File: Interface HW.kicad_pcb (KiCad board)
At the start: 2 copper layers, 101.6 x 50.8 mm, 79 parts, among them J1 CONN_8, J2 CONN_8, J3 CONN_8, J4 CONN_8, J5 TE: 640456-3, J6 CONN_13X2, J7 TERM_3, J8 TERM-3, P1 CONNECTOR_2, Q1 2N7002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

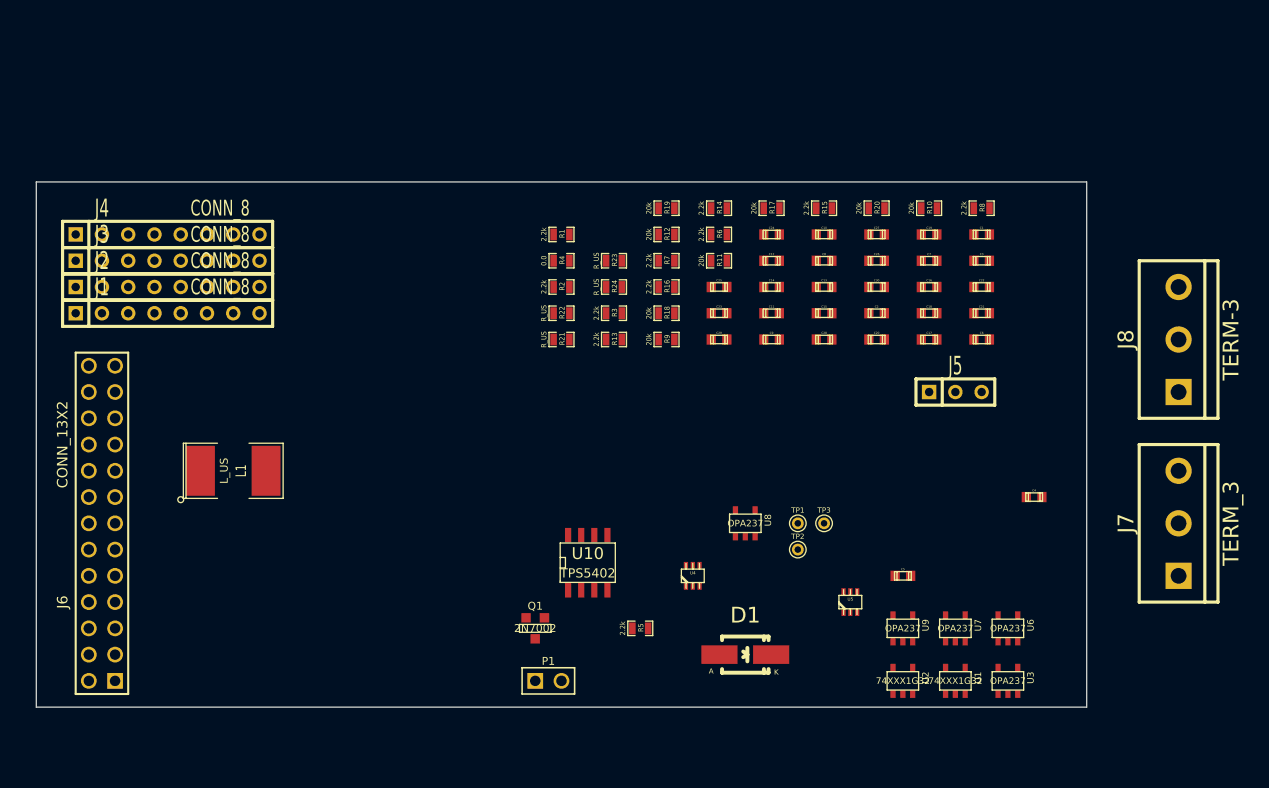
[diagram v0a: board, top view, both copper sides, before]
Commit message: Changed PCB size to 5x5cm, got most components placed
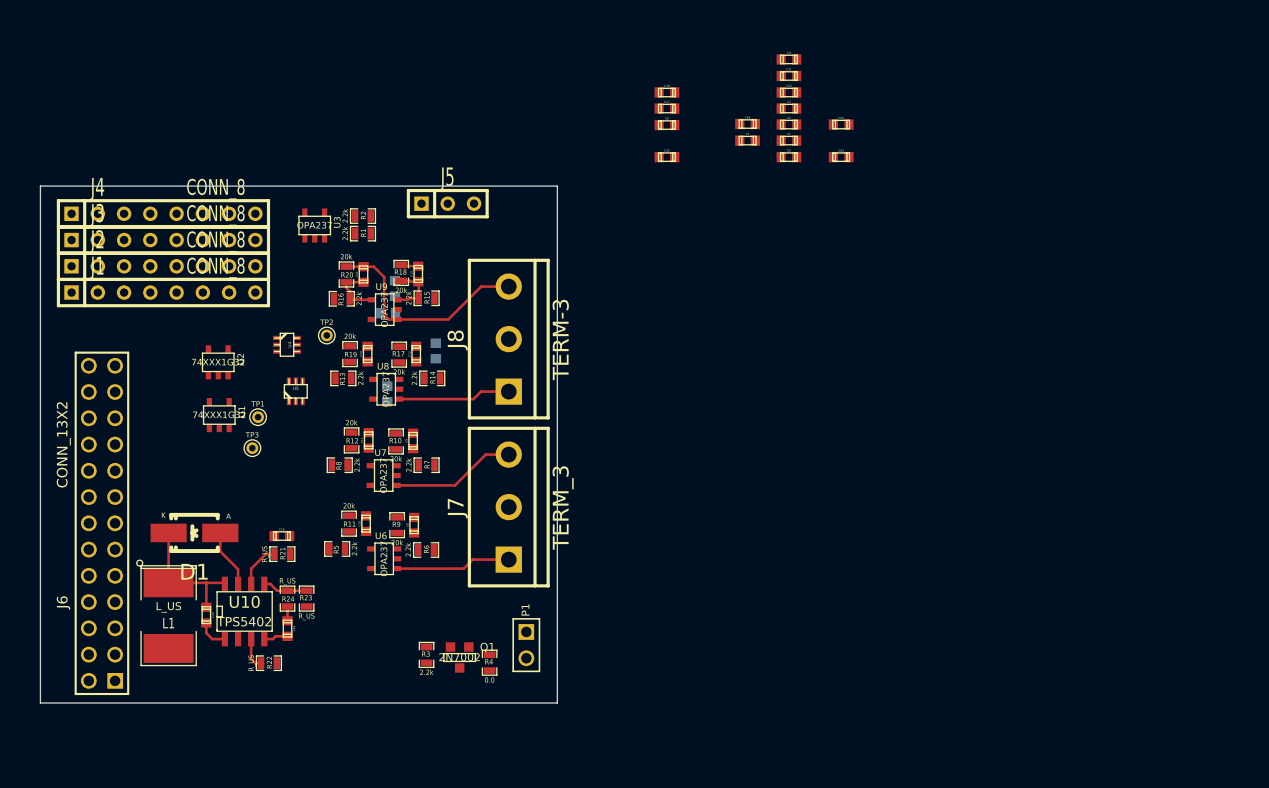
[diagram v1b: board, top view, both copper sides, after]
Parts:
- C27, C28, C29, C30: moved to B.Cu
- moved U3 80.2 mm to (128.5, 105.8)
- moved U1 75.7 mm to (119.3, 124.2)
- moved U2 73.0 mm to (119.2, 119.0)
- moved C19 72.8 mm to (125.9, 144.8), turned to 270 degrees
- moved C20 70.1 mm to (118.0, 143.5), turned to 270 degrees
- moved C16 67.1 mm to (125.3, 135.8)
- moved R8 66.9 mm to (130.9, 129.0), turned to 180 degrees
- moved J7 64.8 mm to (147.3, 133.1)
- moved J8 64.8 mm to (147.3, 116.8)
- moved U6 60.7 mm to (135.2, 138.1), turned to 90 degrees
- moved U9 58.8 mm to (135.3, 114.0), turned to 90 degrees
- moved U5 57.4 mm to (126.7, 121.8)
- moved U7 57.2 mm to (135.2, 130.0), turned to 90 degrees
- moved R10 56.3 mm to (136.4, 126.7), turned to 90 degrees
- moved TP3 55.8 mm to (122.5, 127.3)
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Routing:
- net N-0000062: track 0.00 -> 21.3 mm
- net N-0000069: track 0.00 -> 12.8 mm
- net N-0000055: track 0.00 -> 12.1 mm
- net N-0000061: track 0.00 -> 11.1 mm
- net N-0000067: track 0.00 -> 10.9 mm
- net GND: track 0.00 -> 8.77 mm
- net N-0000065: track 0.00 -> 5.56 mm
- net N-0000063: track 0.00 -> 5.38 mm
- net N-0000070: track 0.00 -> 4.37 mm
- net N-0000071: track 0.00 -> 4.31 mm
- net N-0000072: track 0.00 -> 3.04 mm
- net N-0000068: track 0.00 -> 3.03 mm
- net N-0000073: track 0.00 -> 2.35 mm
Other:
- board size 101.6 x 50.8 mm -> 50 x 50 mm

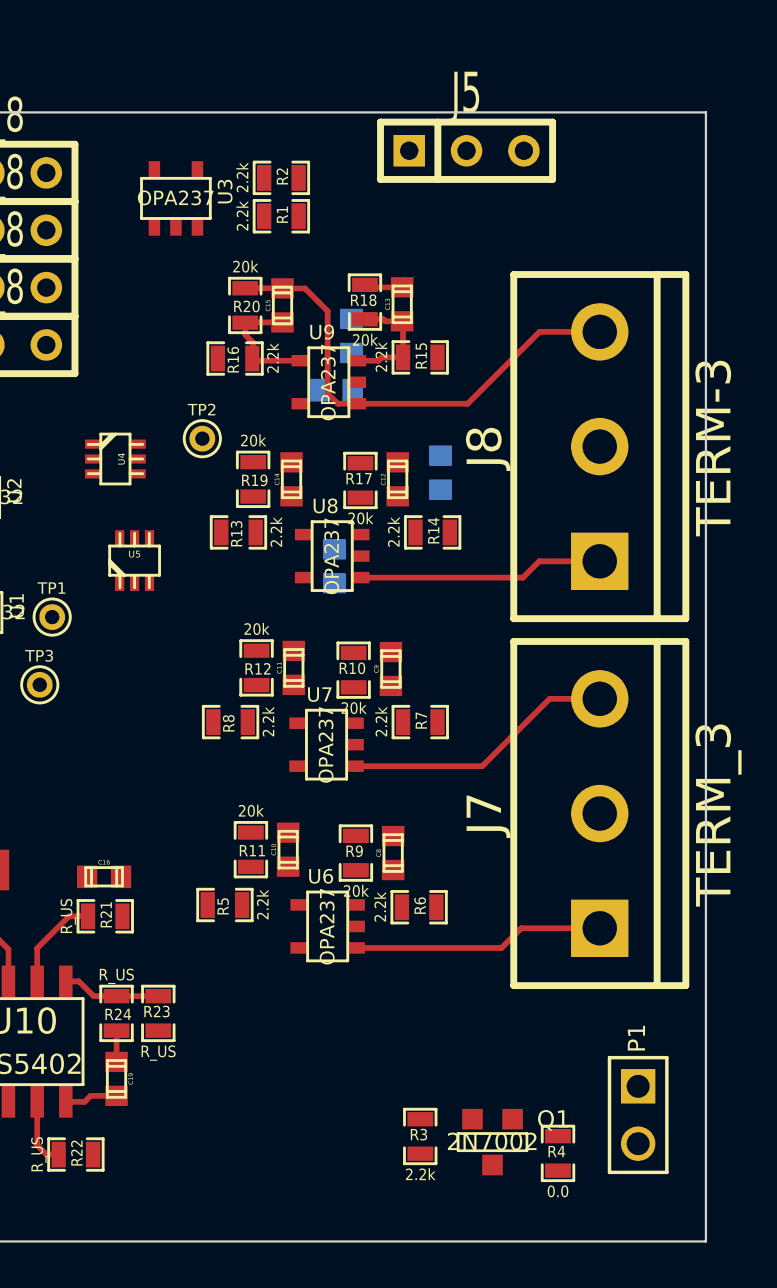
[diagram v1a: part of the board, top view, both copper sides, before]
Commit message: Added a cap to ref, chages buck converter caps, more routing, didn't pull in netlist
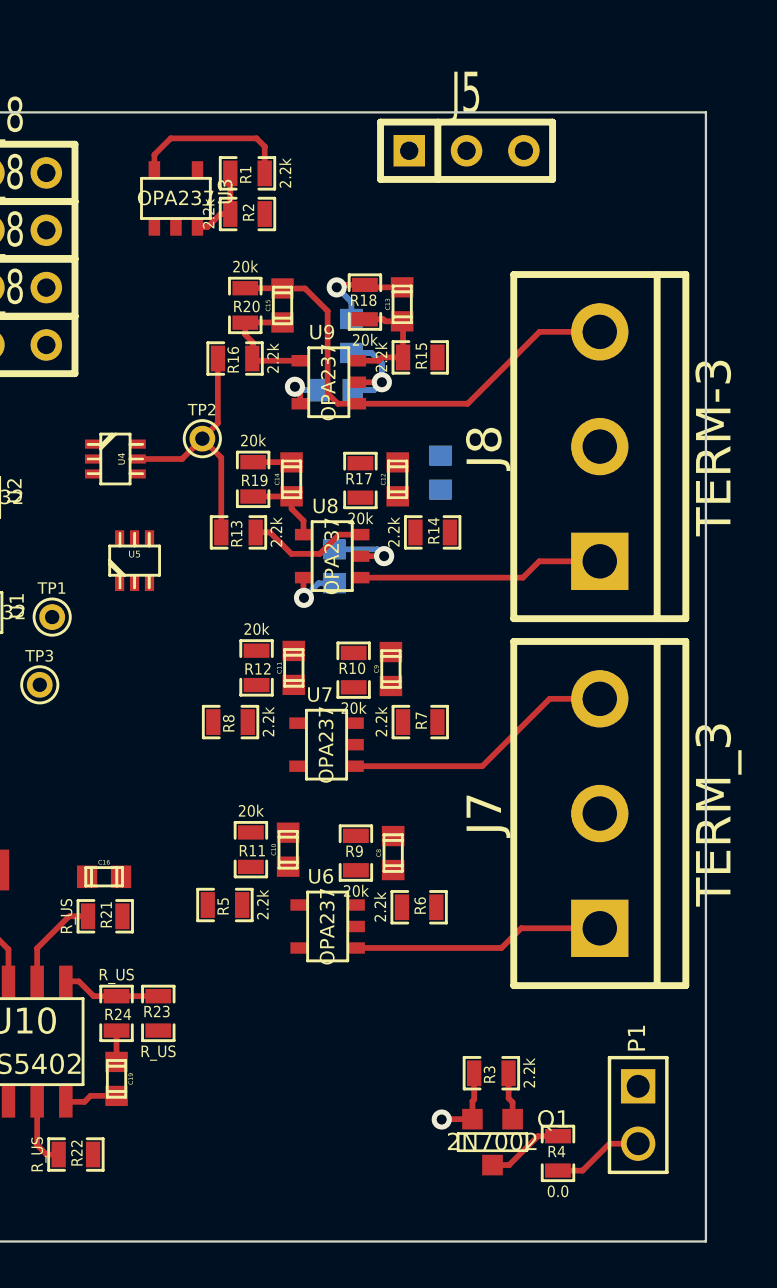
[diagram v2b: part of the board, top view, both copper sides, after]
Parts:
- moved R3 4.21 mm to (142.5, 144.6), turned to 180 degrees
- moved R1 2.42 mm to (131.7, 104.7), turned to 180 degrees
- moved R2 2.19 mm to (131.7, 106.5)
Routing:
- net DAC_Y: track 0.00 -> 11.5 mm
- net -15V: track 0.00 -> 8.26 mm, vias 0 -> 2
- net 3V3: track 0.00 -> 7.19 mm
- net GND: track 8.77 -> 15.4 mm, vias 0 -> 2
- net N-0000064: track 0.00 -> 5.40 mm
- net +15V: track 0.00 -> 4.48 mm, vias 0 -> 2
- net N-0000025: track 0.00 -> 4.04 mm
- net N-0000066: track 0.00 -> 3.62 mm
- net N-0000054: track 0.00 -> 3.50 mm
- net N-0000024: track 0.00 -> 3.43 mm
- net /Interface HW-01/GPIO_12: track 0.00 -> 2.11 mm
- net N-0000067: track 10.9 -> 12.6 mm

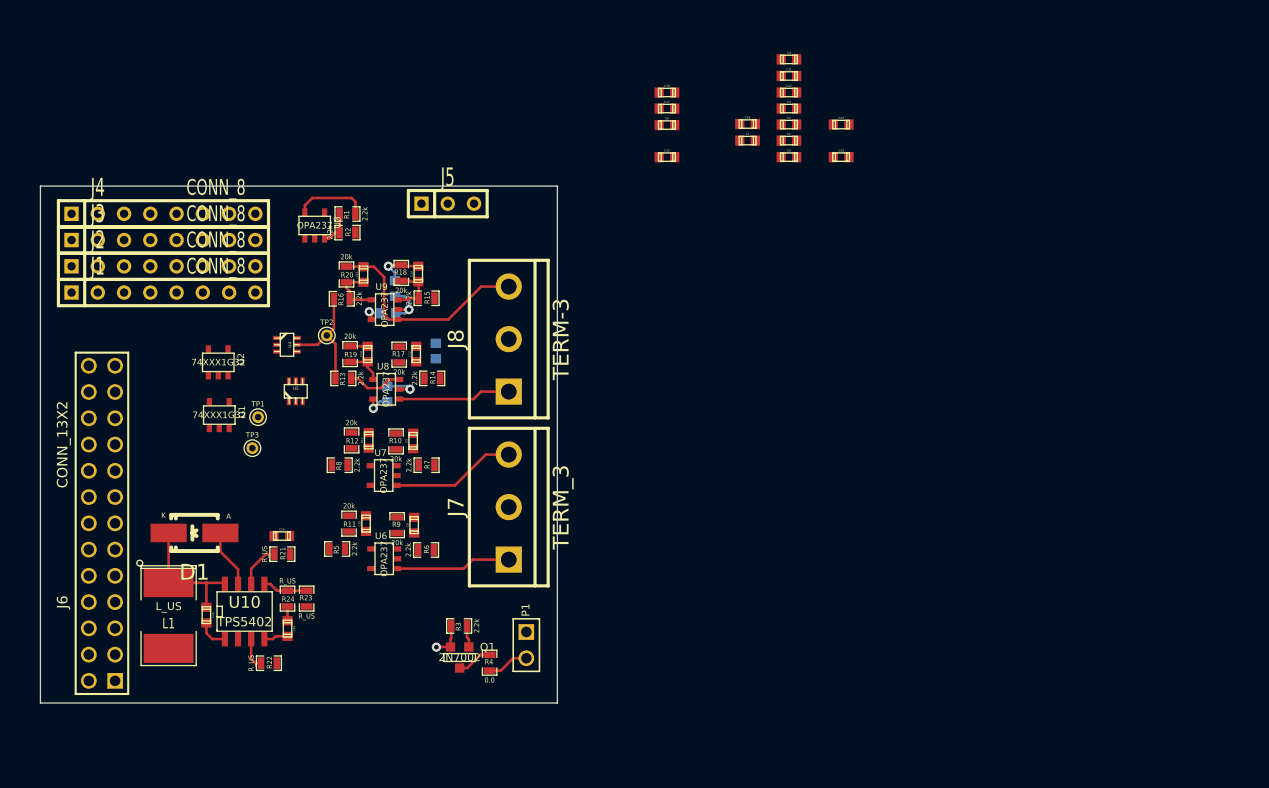
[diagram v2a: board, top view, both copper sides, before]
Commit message: More routing, added power supply test points, added mounting holes
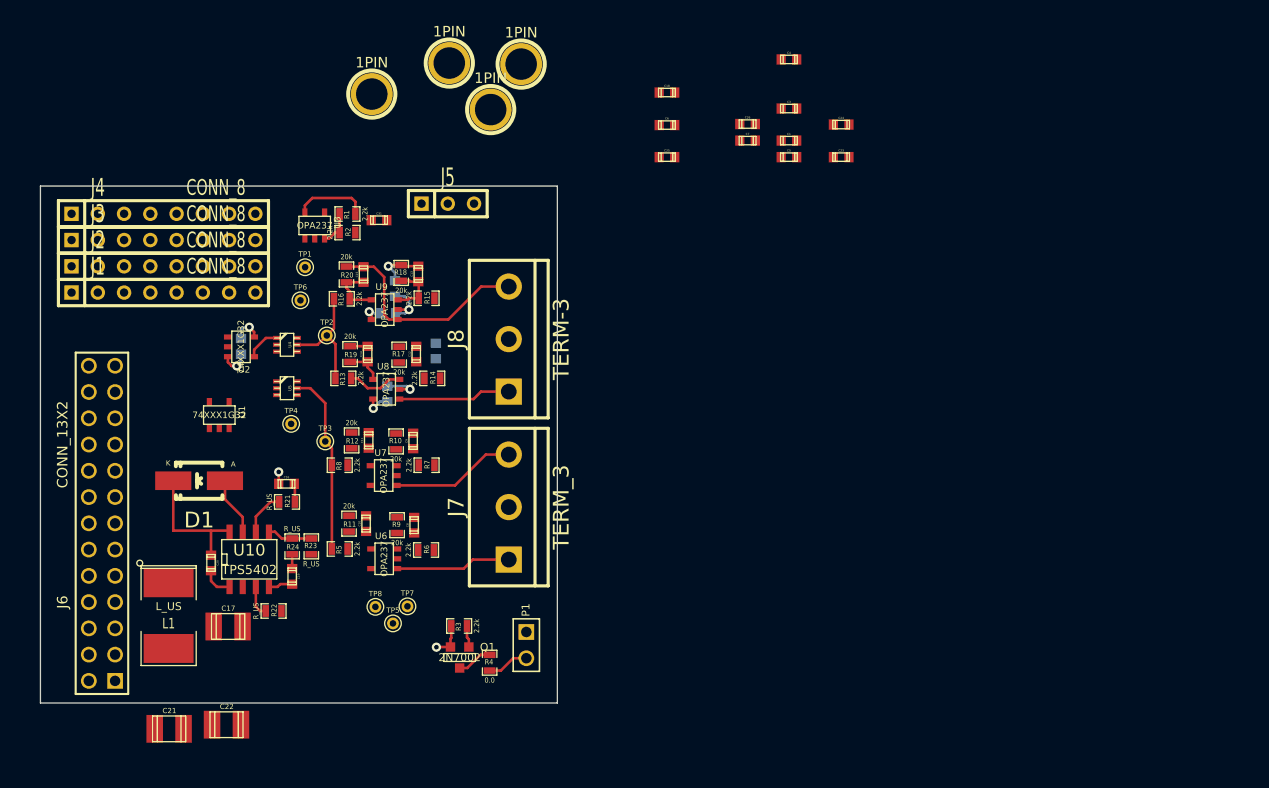
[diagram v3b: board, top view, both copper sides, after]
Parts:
- added 1PIN: P***, 1pin, F.Cu at (134.1, 93.1)
- added 1PIN: P***, 1pin, F.Cu at (141.6, 90.1)
- added 1PIN: P***, 1pin, F.Cu at (148.5, 90.2)
- added 1PIN: P***, 1pin, F.Cu at (145.6, 94.6)
- added C31: 0.1uF, c_0603, F.Cu at (134.8, 105.3)
- added TP4: TEST, PINTST, F.Cu at (126.2, 125.0)
- added TP5: TEST, PINTST, F.Cu at (136.1, 144.3)
- added TP6: TEST, PINTST, F.Cu at (127.2, 113.0)
- added TP7: TEST, PINTST, F.Cu at (137.5, 142.7)
- added TP8: TEST, PINTST, F.Cu at (134.4, 142.7)
- C17, C21, C22: value CSMALL -> 10uF; footprint c_0603 -> c_1210
- C2: moved to B.Cu
- moved C21 87.1 mm to (114.5, 154.5)
- moved C22 81.8 mm to (120.0, 154.1)
- moved C17 65.7 mm to (120.2, 144.6)
- moved C2 57.2 mm to (121.4, 117.5), turned to 90 degrees
- moved TP1 15.2 mm to (127.6, 109.8)
- moved TP3 7.08 mm to (129.6, 126.7)
- moved C20 5.07 mm to (118.5, 138.4)
- moved R22 5.07 mm to (124.5, 143.1)
- moved U10 5.07 mm to (122.2, 138.1)
- moved C19 5.07 mm to (126.3, 139.8)
- moved D1 5.07 mm to (117.3, 130.5)
- moved R23 5.07 mm to (128.2, 136.8)
- moved R24 5.07 mm to (126.3, 136.8)
- moved C16 5.07 mm to (125.8, 130.8)
- moved R21 5.07 mm to (125.8, 132.6)
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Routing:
- net DAC_X: track 0.00 -> 17.6 mm
- net GND: track 15.4 -> 19.5 mm, vias 2 -> 4
- net N-0000053: track 0.00 -> 3.31 mm
- net 3V3: track 7.19 -> 10.1 mm, vias 0 -> 1
- net N-0000074: track 0.00 -> 1.77 mm

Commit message: no unconnected PINSgit status git status
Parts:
- C1, C23, C24, C25, C26, C3, C4, C5: moved to B.Cu
- moved 1PIN 68.5 mm to (104.5, 149.4)
- moved C18 65.7 mm to (119.3, 142.3)
- moved C1 61.6 mm to (116.3, 118.2), turned to 90 degrees
- moved 1PIN 59.9 mm to (149.4, 149.4)
- moved C4 57.2 mm to (128.2, 123.3), turned to 270 degrees
- moved C23 57.1 mm to (135.8, 136.1), turned to 180 degrees
- moved C24 55.7 mm to (135.8, 130.8), turned to 180 degrees
- moved C5 51.3 mm to (126.2, 116.8), turned to 180 degrees
- moved C25 44.4 mm to (132.3, 131.7)
- moved C3 43.4 mm to (132.5, 105.8), turned to 90 degrees
- moved C26 42.3 mm to (138.8, 124.0), turned to 270 degrees
- moved 1PIN 31.6 mm to (104.5, 104.5)
- moved C7 28.7 mm to (143.0, 106.1), turned to 180 degrees
- moved C6 24.8 mm to (139.9, 106.1), turned to 180 degrees
- moved C21 24.6 mm to (123.8, 131.8), turned to 90 degrees
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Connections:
- R14 pad 2: REF_1.65 -> REF_1.65V
- R15 pad 2: REF_1.65 -> REF_1.65V
- R6 pad 2: REF_1.65 -> REF_1.65V
- R7 pad 2: REF_1.65 -> REF_1.65V
- U4 pad 5: DAC_Y -> GND
- U4 pad 6: (no net) -> DAC_Y
- U5 pad 5: DAC_X -> GND
- U5 pad 6: (no net) -> DAC_X
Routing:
- net GND: track 19.5 -> 306.5 mm, vias 4 -> 17
- net 3V3: track 10.1 -> 168.2 mm, vias 1 -> 8
- net /Interface HW-01/GPIO_12: track 2.11 -> 85.7 mm
- net +15V: track 4.48 -> 74.9 mm, vias 2 -> 5
- net -15V: track 8.26 -> 59.9 mm, vias 2 -> 4
- net /Interface HW-01/SPISIMO_A: track 0.00 -> 51.6 mm, vias 0 -> 2
- net REF_1.65V: track 0.00 -> 48.5 mm, vias 0 -> 6
- net /Interface HW-01/SPICLK_A: track 0.00 -> 39.6 mm, vias 0 -> 1
- net /Interface HW-01/SPISTE_A: track 0.00 -> 30.1 mm, vias 0 -> 3
- net /Interface HW-01/SDA_A: track 0.00 -> 23.5 mm
- net N-0000059: track 0.00 -> 19.9 mm
- net /Interface HW-01/SCL_A: track 0.00 -> 19.2 mm
- net N-0000066: track 12.6 -> 26.6 mm, vias 0 -> 2
- net N-0000057: track 0.00 -> 13.6 mm, vias 0 -> 2
- net N-0000065: track 3.62 -> 16.4 mm
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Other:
- net class Default: clearance 0.254 -> 0.1524; trace_width 0.254 -> 0.1524
- rule trace_clearance: 0.254 -> 0.1524
- rule trace_min: 0.254 -> 0.1524

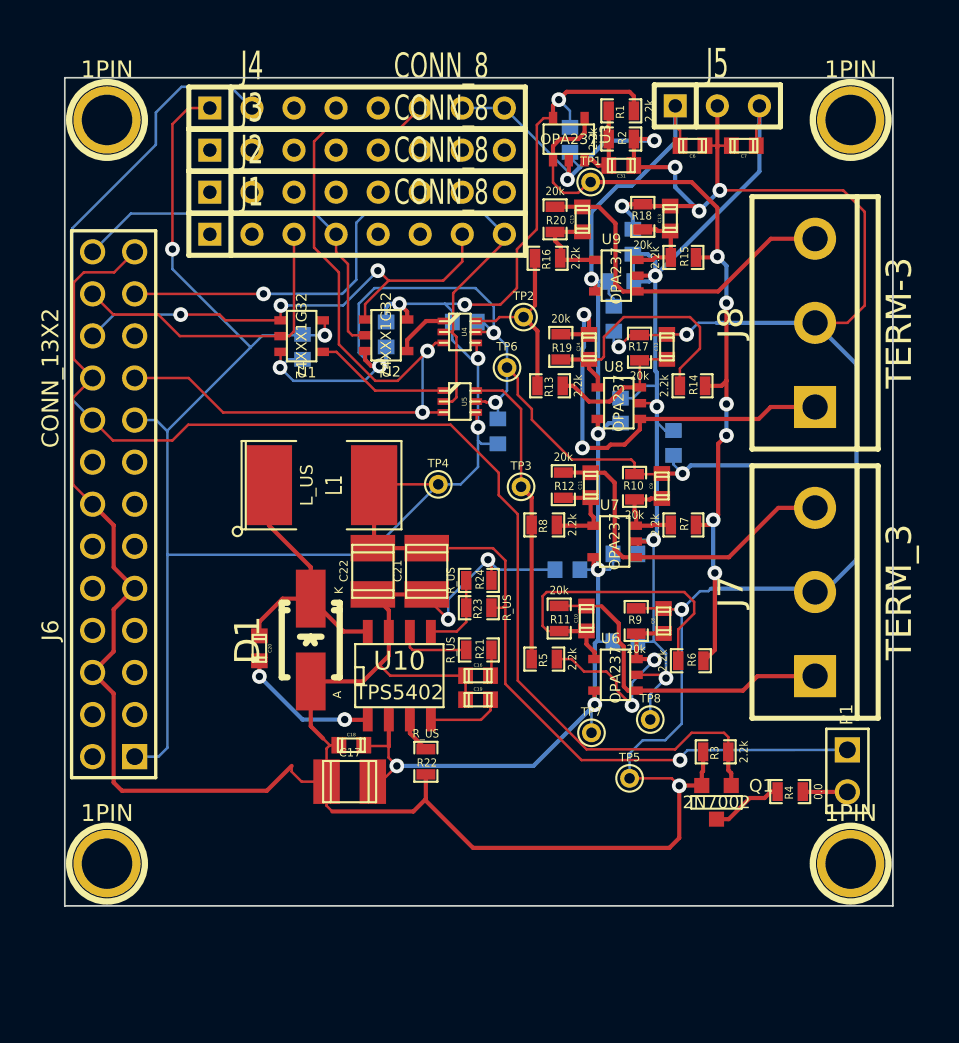
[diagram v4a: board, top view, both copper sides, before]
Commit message: Silk cleanup
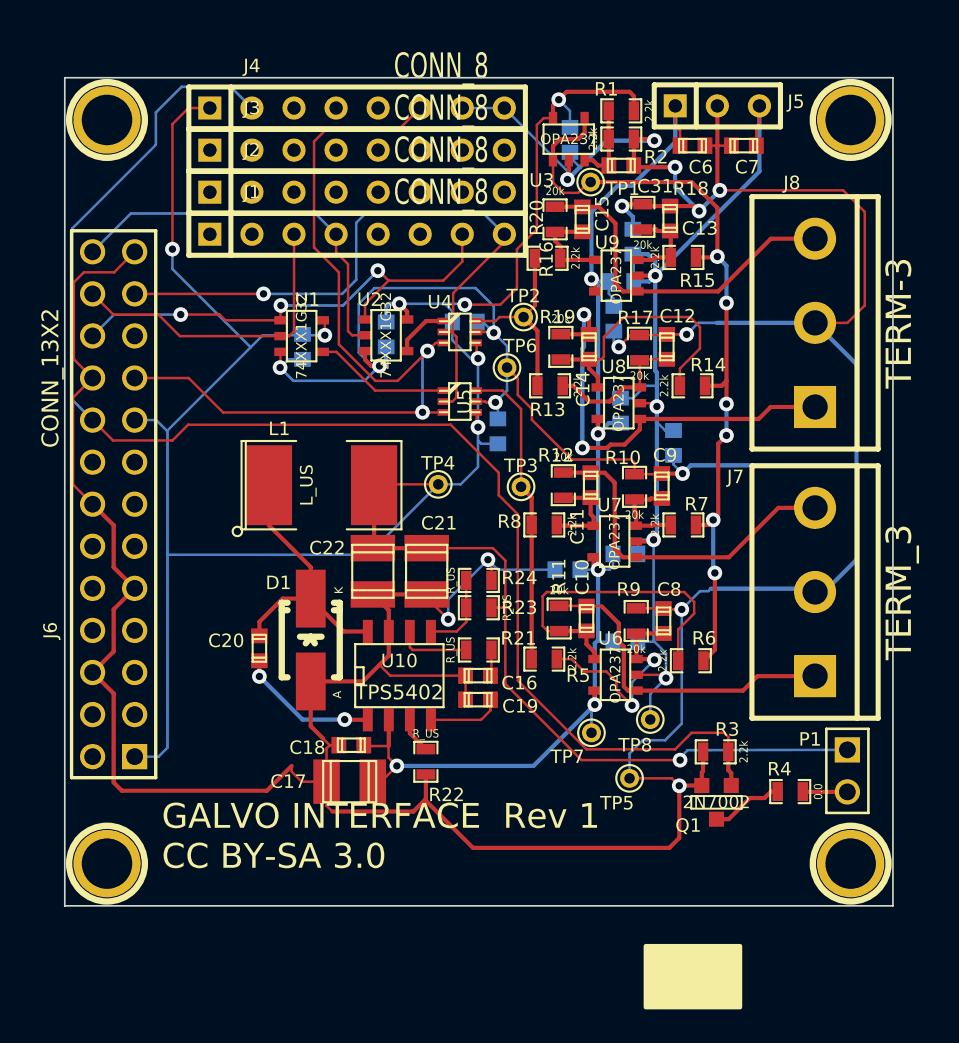
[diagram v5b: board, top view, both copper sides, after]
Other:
- board text added: "GALVO INTERFACE Rev 1 CC BY-SA 3.0"

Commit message: Added OSHW logo
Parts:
- added G***: LOGO, OSHWLOGO0.3IN, F.Cu at (140.1, 145.3)
